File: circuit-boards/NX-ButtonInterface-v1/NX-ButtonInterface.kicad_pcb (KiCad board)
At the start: 2 copper layers, 48.3 x 21.2 mm, 3 parts, among them J1 NX CONTROL & UART, J2 NX-BUTTON, J4 POWER LED

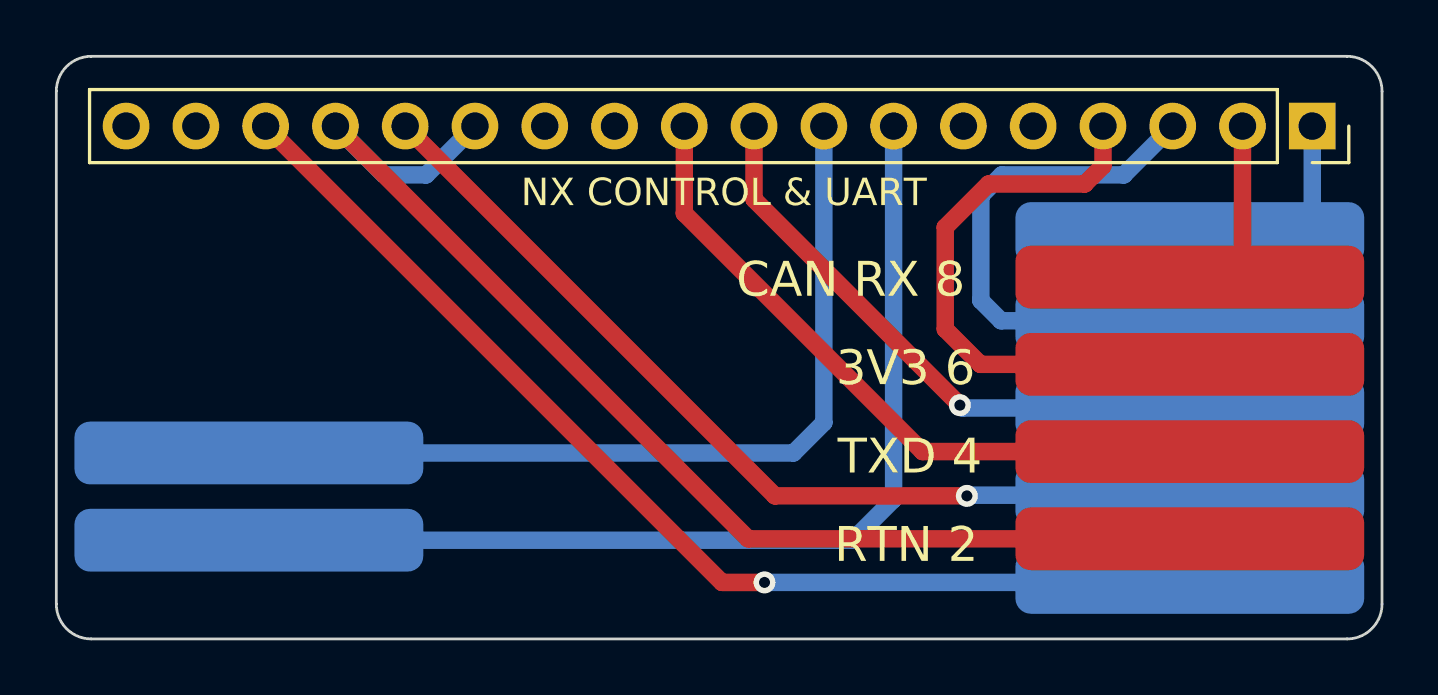
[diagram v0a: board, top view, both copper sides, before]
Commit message: Update NX-J401 and NX Button Interface boards
Signed-off-by: Scott Berman <scott.berman@bluerivertech.com>
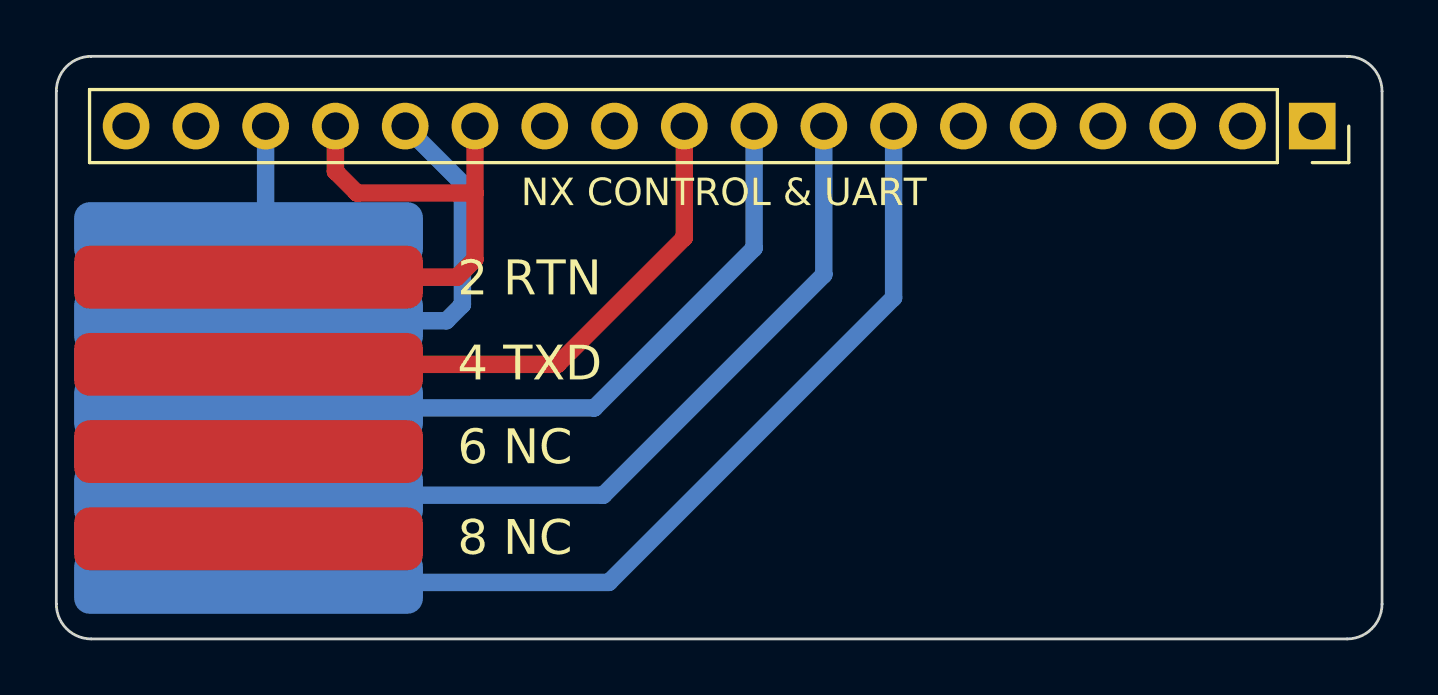
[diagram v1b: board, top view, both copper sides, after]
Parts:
- removed J4: POWER LED, NX-ButtonInterface:2-pin-solder-pads
- moved J2 36.5 mm to (91.2, 96.9), turned to 180 degrees
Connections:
- J2 pad 6: /3V3 -> unconnected-(J2-Pin_6-Pad6)
- J2 pad 7: /GND -> /NX_PC_LED+
- J2 pad 8: /CAN_RX -> unconnected-(J2-Pin_8-Pad8)
- J2 pad 9: /CAN_TX -> /NX_PC_LED-
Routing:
- net /~{REC}: track 40.5 -> 4.17 mm, vias 1 -> 0
- net /SYS_RST_RCV_RTN: track 43.9 -> 20.4 mm
- net /3V3: track 21.3 -> 0.00 mm
- net /GND: track 19.8 -> 0.00 mm
- net /~{SYS_RESET}: track 34.1 -> 15.4 mm, vias 1 -> 0
- net /CAN_TX: track 11.4 -> 0.00 mm
- net /CAN_RX: track 7.38 -> 0.00 mm
- net /NX_PC_LED-: track 37.7 -> 34.0 mm
- net /UART2_RXD: track 21.7 -> 25.3 mm, vias 1 -> 0
- net /UART2_TXD: track 25.2 -> 21.8 mm
- net /NX_PC_LED+: track 32.2 -> 29.7 mm
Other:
- board text added: "1. Layer Count: 2 2. PCB Thickness: 1.6 mm 3. PCB Color: Green 4. Surface Finish: HASL (with lead) 5. Outer Copper Weight: 1 oz. 6. Via Covering: Tented 7. Board Outline Tolerance: +/-0.2mm"
- board text added: "2 RTN"
- board text added: "4 TXD"
- board text added: "58.45669 mils"
- board text added: "6 NC"
- board text added: "62.00 mils"
- board text added: "8 NC"
- board text added: "LED+ 7"
- board text added: "LED- 9"
- board text added: "RXD 5"
- board text added: "~{REC} 1"
- board text added: "~{RESET} 3"
- board text removed: "1 ~{REC}"
- board text removed: "1. Layer Count: 2 2. PCB Thickness: 0.8 mm 3. PCB Color: Green 4. Surface Finish: HASL (with lead) 5. Outer Copper Weight: 1 oz. 6. Via Covering: Tented 7. Board Outline Tolerance: +/-0.2mm"
- board text removed: "27.95276 mils"
- board text removed: "3 ~{RESET}"
- board text removed: "31.50 mils"
- board text removed: "3V3 6"
- board text removed: "5 RXD"
- board text removed: "7 GND"
- board text removed: "9 CAN TX"
- board text removed: "CAN RX 8"
- board text removed: "LED+ 1"
- board text removed: "LED- 2"
- board text removed: "RTN 2"
- board text removed: "TXD 4"
